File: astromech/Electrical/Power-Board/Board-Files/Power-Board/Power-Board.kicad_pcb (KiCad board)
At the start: 2 copper layers, 119.4 x 96.5 mm, 66 parts, among them J1 BAT_IN_SCREW, J10 HEAD_MOT, J2 BAT_IN_HOLE, J5 E_STOP, J6 CTRL_BRD, J7 JETSON, J8 L_DRIVE, J9 R_DRIVE, Q1 Q_NMOS_DSG, Q2 Q_NMOS_DSG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

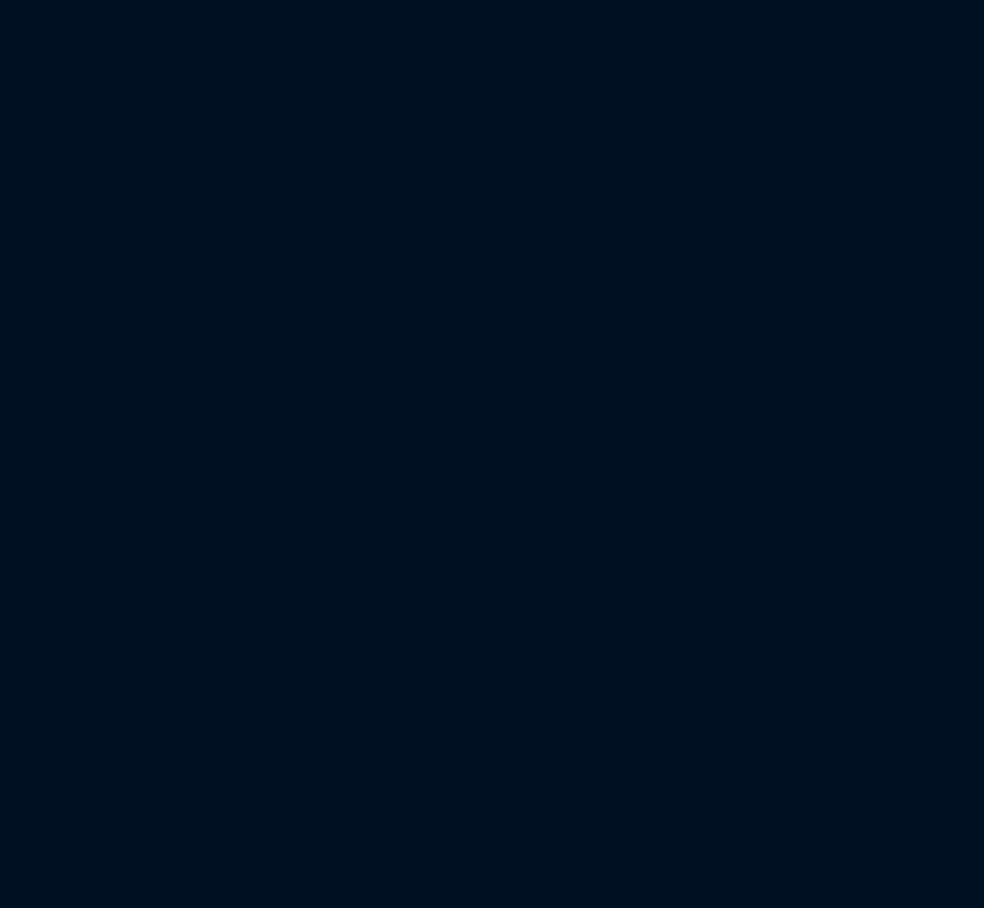
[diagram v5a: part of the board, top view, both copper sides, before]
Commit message: Applied generic fuse footprints
Assigned generic fuse footprint to resettable fuses, and updated layout to include these newly assigned footprints
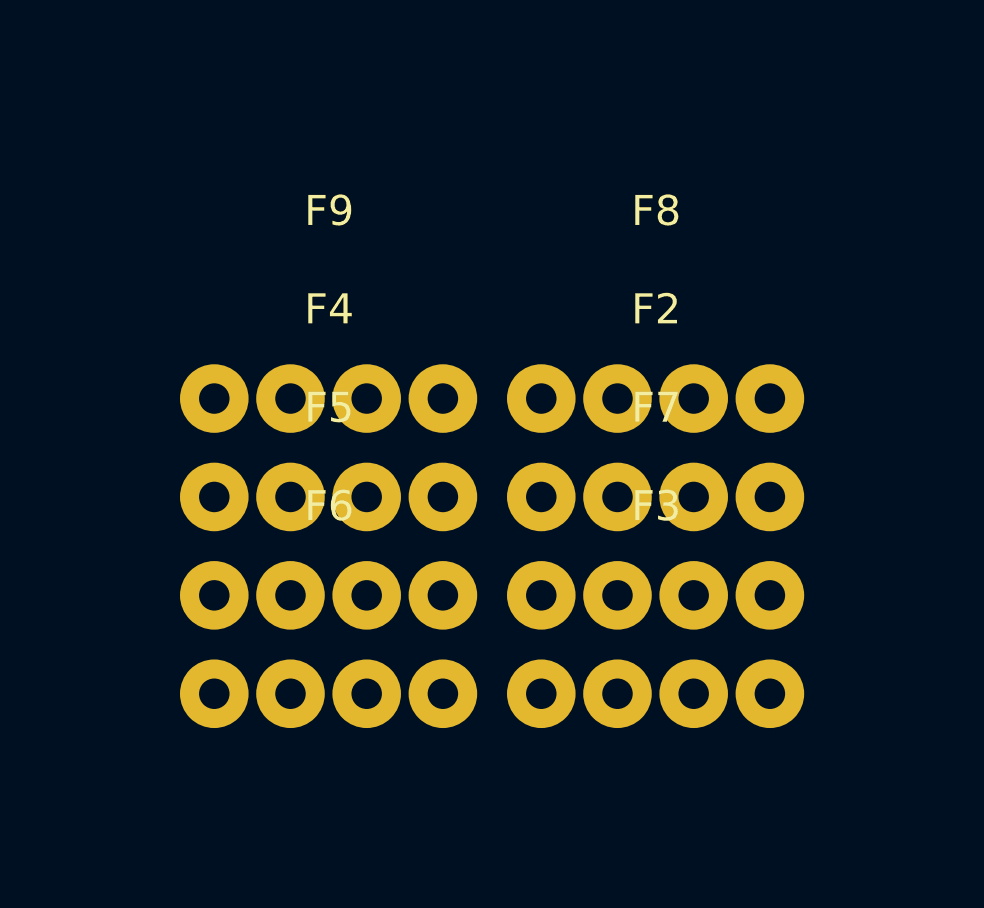
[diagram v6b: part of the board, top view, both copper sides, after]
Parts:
- added F2: F_12V, astromech-footprints:Generic-Fuse, F.Cu at (239.4, 28.6)
- added F3: F_5V, astromech-footprints:Generic-Fuse, F.Cu at (239.4, 35.1)
- added F4: F_3V, astromech-footprints:Generic-Fuse, F.Cu at (228.5, 28.6)
- added F5: F_CTRL, astromech-footprints:Generic-Fuse, F.Cu at (228.5, 31.9)
- added F6: F_JETSON, astromech-footprints:Generic-Fuse, F.Cu at (228.5, 35.1)
- added F7: F_LDRIVE, astromech-footprints:Generic-Fuse, F.Cu at (239.4, 31.9)
- added F8: F_RDRIVE, astromech-footprints:Generic-Fuse, F.Cu at (239.4, 25.3)
- added F9: F_HEADMOT, astromech-footprints:Generic-Fuse, F.Cu at (228.5, 25.3)

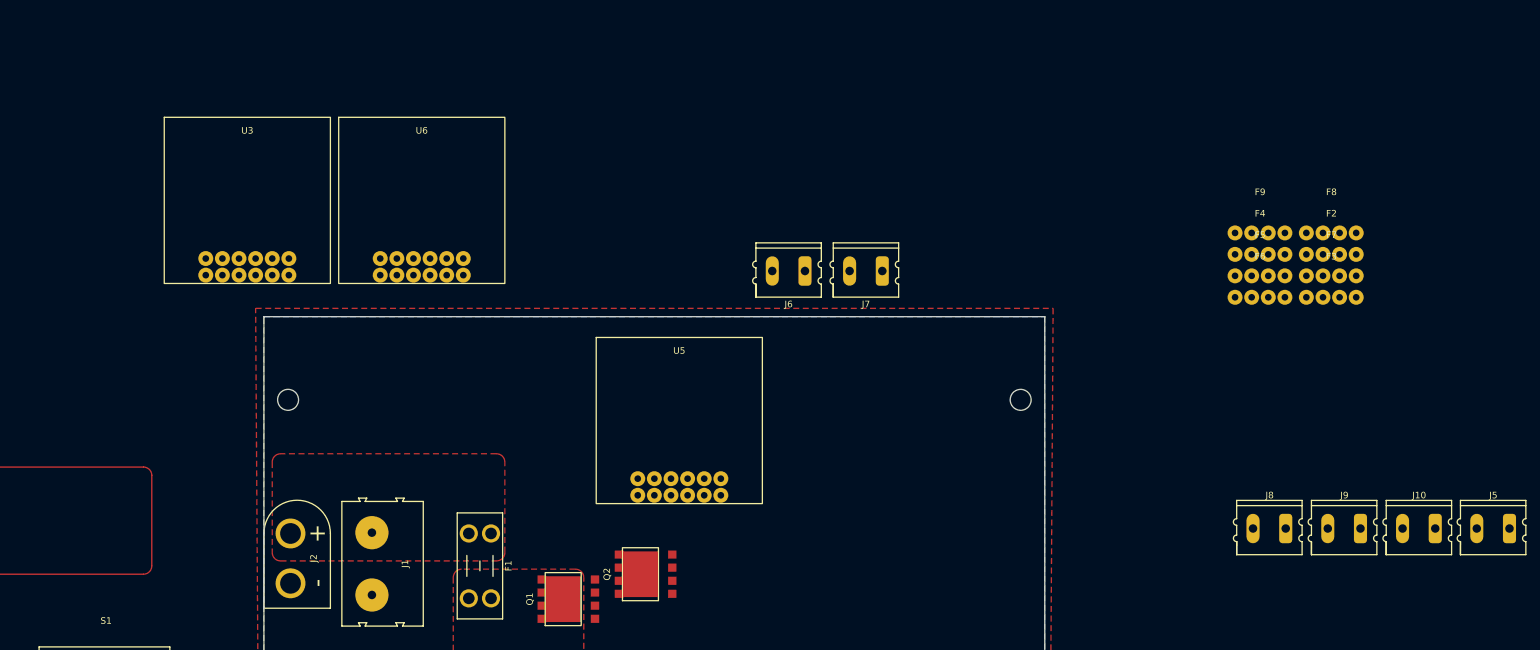
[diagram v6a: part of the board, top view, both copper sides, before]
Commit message: minor layout changes
added trace to motor mosfet
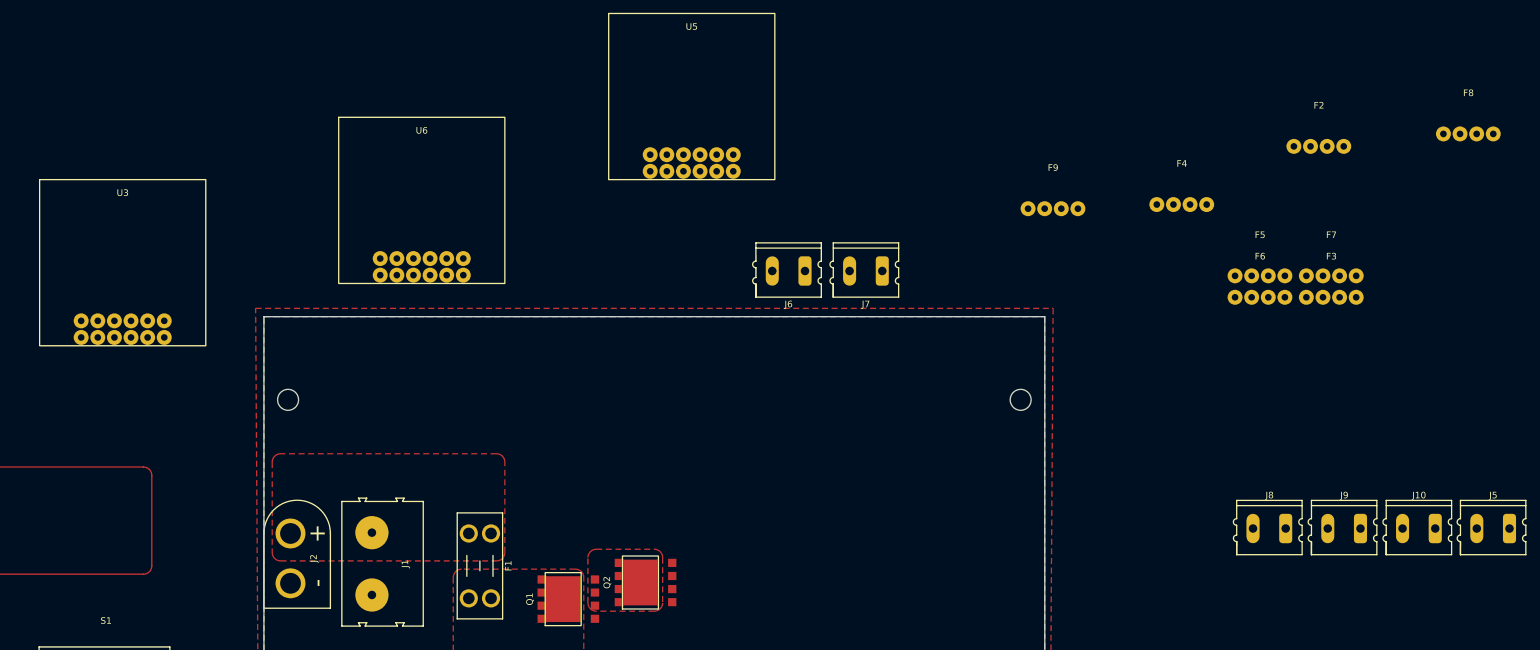
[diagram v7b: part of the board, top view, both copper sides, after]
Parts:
- moved U5 49.6 mm to (141.6, 4.45)
- moved F9 31.9 mm to (196.8, 21.6)
- moved F8 25.8 mm to (260.4, 10.2)
- moved U3 21.3 mm to (54.6, 29.8)
- moved F2 16.6 mm to (237.5, 12.1)
- moved F4 14.2 mm to (216.5, 21.0)
- moved Q2 1.27 mm to (134.6, 78.7)
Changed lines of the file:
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@@
   )
   (footprint "astromech-footprints:Generic-Fuse" (layer "F.Cu")
-    (at 228.495 28.575)
+    (at 216.535 20.955)
     (property "Sheetfile" "Power-Board.kicad_sch")
     (property "Sheetname" "")
@@
   )
   (footprint "astromech-footprints:Generic-Fuse" (layer "F.Cu")
-    (at 239.395 28.575)
+    (at 237.49 12.065)
     (property "Sheetfile" "Power-Board.kicad_sch")
     (property "Sheetname" "")
@@
   )
   (footprint "astromech-footprints:D36V50Fx" (layer "F.Cu")
-    (at 73.66 20.32)
+    (at 54.61 29.845)
     (property "Sheetfile" "Power-Board.kicad_sch")
     (property "Sheetname" "")
@@
   )
   (footprint "astromech-footprints:D36V50Fx" (layer "F.Cu")
-    (at 139.7 53.975)
+    (at 141.605 4.445)
     (property "Sheetfile" "Power-Board.kicad_sch")
     (property "Sheetname" "")
@@
   )
   (footprint "astromech-footprints:Generic-Fuse" (layer "F.Cu")
-    (at 239.395 25.295)
+    (at 260.35 10.16)
     (property "Sheetfile" "Power-Board.kicad_sch")
     (property "Sheetname" "")
@@
   )
   (footprint "astromech-footprints:Generic-Fuse" (layer "F.Cu")
-    (at 228.495 25.295)
+    (at 196.85 21.59)
     (property "Sheetfile" "Power-Board.kicad_sch")
     (property "Sheetname" "")
@@
   )
   (footprint "astromech-footprints:NTMTS0D6N04CLTXG" (layer "F.Cu")
-    (at 134.62 77.47 90)
+    (at 134.62 78.74 90)
     (property "Sheetfile" "Power-Board.kicad_sch")
     (property "Sheetname" "")
@@
       (polygon
         (pts
-          (xy 131.01 81.52)
-          (xy 131.01 73.42)
-          (xy 136.51 73.42)
-          (xy 136.51 81.52)
+          (xy 131.01 82.79)
+          (xy 131.01 74.69)
+          (xy 136.51 74.69)
+          (xy 136.51 82.79)
         )
       )
@@
       )
     )
+  )
+  (zone (net 9) (net_name "+BATT") (layer "F.Cu") (hatch edge 0.508)
+    (connect_pads yes (clearance 0.508))
+    (min_thickness 0.254) (filled_areas_thickness no)
+    (fill yes (thermal_gap 0.508) (thermal_bridge_width 0.508))
+    (polygon
+      (pts
+        (arc (start 125.73 74.93) (mid 126.101974 74.031974) (end 127 73.66))
+        (arc (start 135.89 73.66) (mid 136.788026 74.031974) (end 137.16 74.93))
+        (arc (start 137.16 81.8515) (mid 136.788026 82.749526) (end 135.89 83.1215))
+        (arc (start 127 83.1215) (mid 126.101975 82.749525) (end 125.73 81.8515))
+      )
+    )

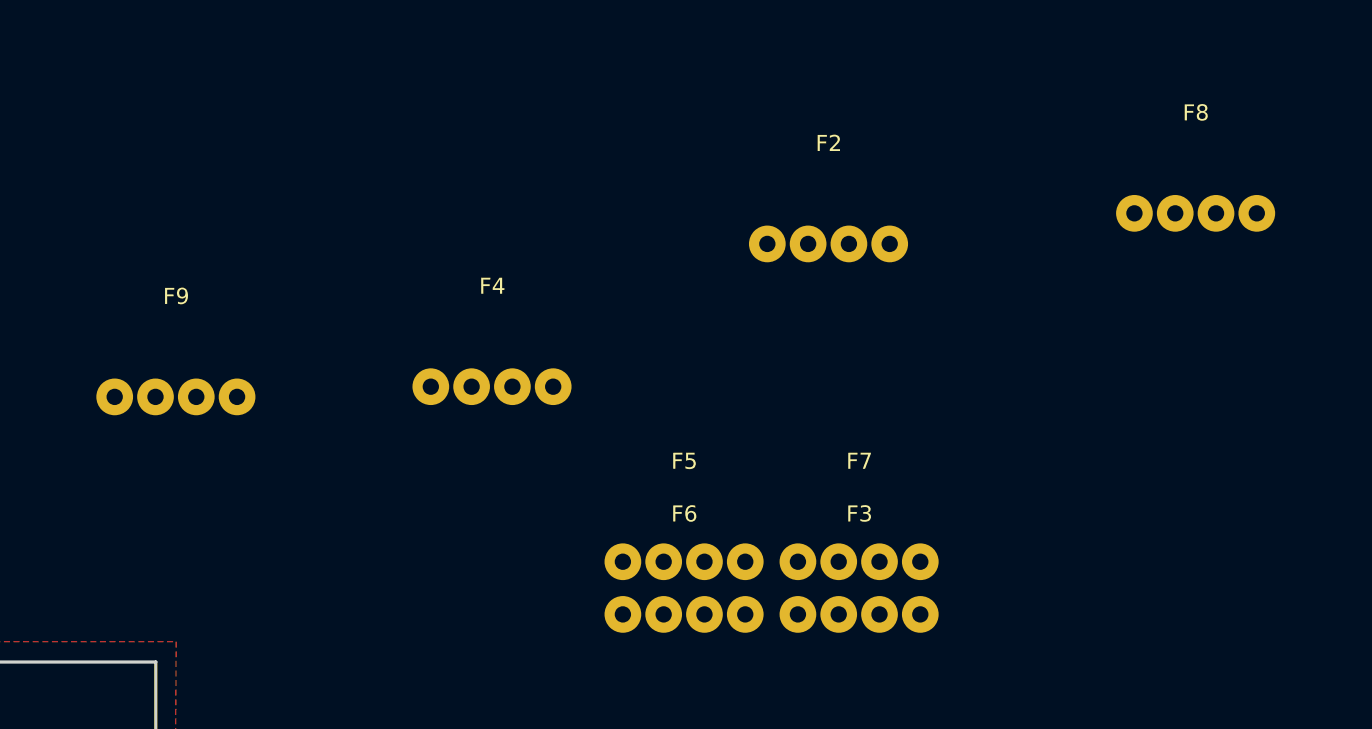
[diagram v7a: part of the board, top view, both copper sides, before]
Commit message: Updated generic fuse footprint
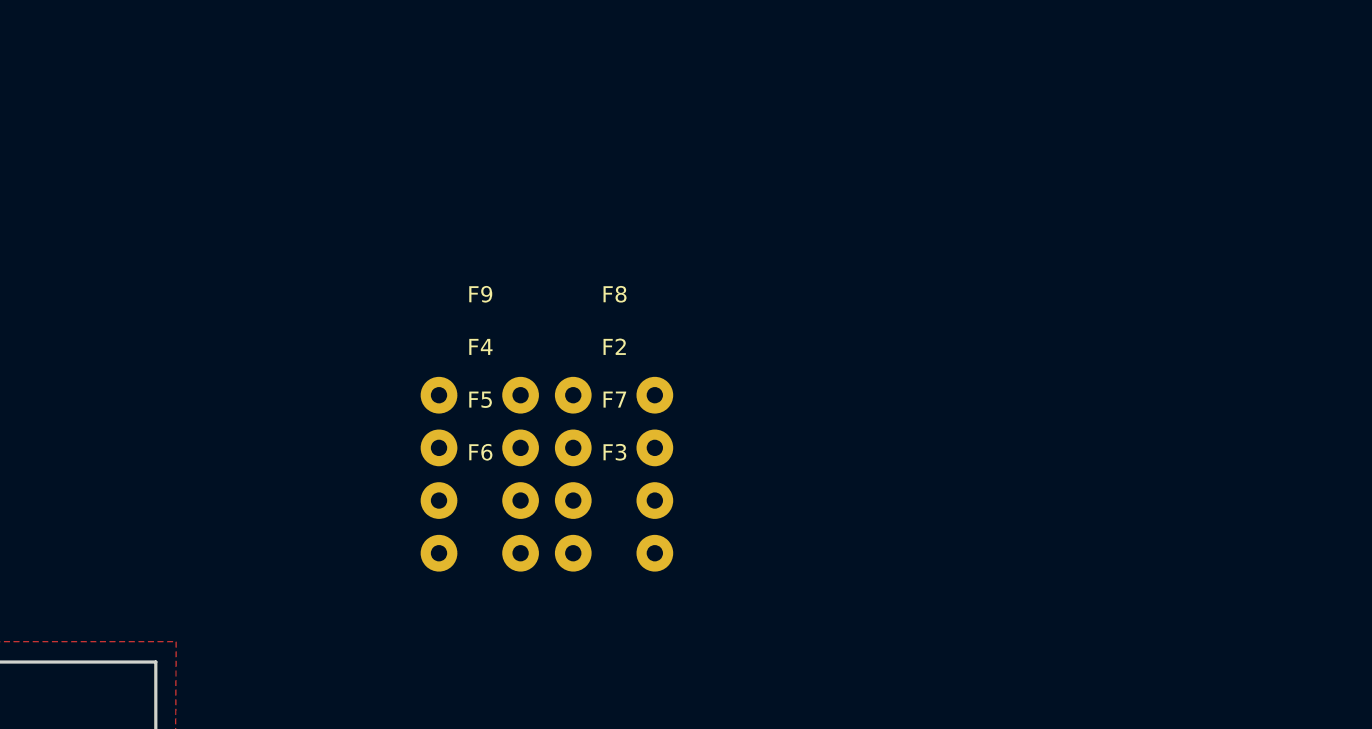
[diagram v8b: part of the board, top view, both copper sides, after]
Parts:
- moved F8 37.9 mm to (224.2, 21.5)
- moved F9 18.9 mm to (215.8, 21.5)
- moved F2 18.4 mm to (224.2, 24.8)
- moved F3 15.7 mm to (224.2, 31.3)
- moved F7 15.7 mm to (224.2, 28.0)
- moved F5 13.3 mm to (215.8, 28.0)
- moved F6 13.3 mm to (215.8, 31.3)
- moved F4 3.88 mm to (215.8, 24.8)
